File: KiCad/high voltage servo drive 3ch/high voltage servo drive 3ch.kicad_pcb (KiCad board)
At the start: 4 copper layers, 111.2 x 227 mm, 483 parts, among them J1 8P8C_LED_Shielded_x2, J3 Conn_ARM_SWD_TagConnect_TC2030, J4 MOTOR_A, J5 MOTOR_B, J6 MOTOR_C, J7 DC BUS, J8 STO, M1 Fan_4pin, Q1 BSS83P, U1 STM32G473QET6, U10 TPS54202DDC, U11 TPS54202DDC, U12 OPA4323IPWR, U13 OPA4323IPWR, U14 OPA4323IPWR, U15 PC-817S1-CTP1-F, U16 PC-817S1-CTP1-F, U17 IPM, U18 IPM, U19 PC-817S1-CTP1-F, U2 IPM, U3 MAX13433EESD, U4 MAX13433EESD, U5 CA_IS3741HW, U6 R24C2T25-R, U7 CA_IS3741HW, U8 CA_IS3741HW, U9 74LVC1G126, X1 SG-8002CE

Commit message: prepare rev0.1 for manufacturing
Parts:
- removed C137: 2.2uf, Capacitor_SMD:C_1206_3216Metric
- removed C45: 22uf, Capacitor_SMD:CP_Elec_6.3x5.9
- removed C46, C47: .1uf, Capacitor_SMD:C_0402_1005Metric
- removed C48: 75pf, Capacitor_SMD:C_0402_1005Metric
- removed C49, C50, C51: 22uf, Capacitor_SMD:C_1206_3216Metric
- removed C52: 220pf, Capacitor_THT:C_Disc_D9.0mm_W5.0mm_P10.00mm
- removed FB3, FB4: FerriteBead, Inductor_SMD:L_0805_2012Metric
- removed H1, H2, H3, H4, H5, H6, H7, H8, H9: MountingHole, footprints:MountingHole_3.2mm_M3
- removed L6: 15uH, Inductor_SMD:L_Taiyo-Yuden_MD-4040
- removed R16: 68.1k, Resistor_SMD:R_0402_1005Metric
- removed R25: 500k, Resistor_SMD:R_0402_1005Metric
- removed R26, R27: 100k, Resistor_SMD:R_0402_1005Metric
- removed R28: 13.3k, Resistor_SMD:R_0402_1005Metric
- removed U11: TPS54202DDC, Package_TO_SOT_SMD:SOT-23-6
- added C204: 22uf, Capacitor_SMD:C_1206_3216Metric, F.Cu at (190.2, 262.9)
- added C205: .1uf, Capacitor_SMD:C_0402_1005Metric, F.Cu at (196.4, 251.6)
- added C206: 22uf, Capacitor_SMD:C_1206_3216Metric, F.Cu at (195.5, 265.2)
- added C207: .1uf, Capacitor_SMD:C_1812_4532Metric, F.Cu at (189.5, 244.8)
- added D52: ES1J, Diode_SMD:D_SMA, F.Cu at (188.2, 251.4)
- added D53: ES1J, Diode_SMD:D_SMA, F.Cu at (194.9, 262.1)
- added D54: LED, LED_SMD:LED_0603_1608Metric, F.Cu at (245.1, 96.6)
- added L9: L, Inductor_THT:L_Radial_D7.2mm_P3.00mm_Murata_1700, B.Cu at (192.5, 258.5)
- added PS1: F0505S-1W, footprints:Converter_DCDC_FXXS-1W, B.Cu at (229.0, 56.9)
- added R150: 10k, Resistor_SMD:R_0402_1005Metric, F.Cu at (197.5, 253.7)
- added R151: 120, Resistor_SMD:R_0402_1005Metric, F.Cu at (252.4, 119.7)
- added R152: 1k, Resistor_SMD:R_0402_1005Metric, F.Cu at (196.4, 253.7)
- added R153: 0, Resistor_SMD:R_0402_1005Metric, F.Cu at (224.3, 58.6)
- added R154: 0, Resistor_SMD:R_0402_1005Metric, F.Cu at (222.8, 57.1)
- added R155: 0, Resistor_SMD:R_0402_1005Metric, F.Cu at (222.8, 55.6)
- added R156: 0, Resistor_SMD:R_0402_1005Metric, F.Cu at (226.4, 54.9)
- added REF**: Symbol_HighVoltage_Triangle_8x7mm_Silk, EO logos:Symbol_HighVoltage_Triangle_8x7mm_Silk, F.Cu at (177.3, 200.6)
- added REF**: Symbol_HighVoltage_Triangle_8x7mm_Silk, EO logos:Symbol_HighVoltage_Triangle_8x7mm_Silk, B.Cu at (259.4, 199.1)
- added REF**: Symbol_HighVoltage_Triangle_8x7mm_Silk, EO logos:Symbol_HighVoltage_Triangle_8x7mm_Silk, B.Cu at (192.9, 270.2)
- added REF**: Symbol_HighVoltage_Triangle_8x7mm_Silk, EO logos:Symbol_HighVoltage_Triangle_8x7mm_Silk, F.Cu at (186.9, 82.8)
- added REF**: Symbol_HighVoltage_Triangle_8x7mm_Silk, EO logos:Symbol_HighVoltage_Triangle_8x7mm_Silk, F.Cu at (260.0, 104.8)
- added REF**: Symbol_HighVoltage_Triangle_8x7mm_Silk, EO logos:Symbol_HighVoltage_Triangle_8x7mm_Silk, F.Cu at (169.2, 267.4)
- added REF**: EO silk 14mm, EO logos:EO silk 14mm, F.Cu at (176.7, 78.7)
- added REF**: OSHW-Logo2_14.6x12mm_SilkScreen, Symbol:OSHW-Logo2_14.6x12mm_SilkScreen, F.Cu at (164.0, 87.3)
- added REF**: Symbol_HighVoltage_Triangle_8x7mm_Silk, EO logos:Symbol_HighVoltage_Triangle_8x7mm_Silk, B.Cu at (251.6, 72.1)
- added REF**: OSHW-Logo2_14.6x12mm_SilkScreen, Symbol:OSHW-Logo2_14.6x12mm_SilkScreen, B.Cu at (241.3, 53.6)
- added REF**: EO silk 14mm, EO logos:EO silk 14mm, B.Cu at (255.9, 52.9)
- added TP3: 5V, TestPoint:TestPoint_Pad_D2.0mm, F.Cu at (245.0, 94.1)
- added U20: LNK306D, Package_SO:PowerIntegrations_SO-8C, F.Cu at (193.1, 251.3)
- added U21: TLV75733PDBV, Package_TO_SOT_SMD:SOT-23-5, F.Cu at (246.9, 105.6)
- C101, C107, C109, C56, C57, C64, C70, C76, C82, C88, C90, C95: value 0.1uf -> .1uf
- C127: value 75pf -> 100pf
- C130: footprint Capacitor_THT:C_Rect_L18.0mm_W11.0mm_P15.00mm_FKS3_FKP3 -> Capacitor_THT:C_Rect_L26.5mm_W10.5mm_P22.50mm_MKS4
- C24: value 330pf -> 22uf; footprint Capacitor_SMD:C_0402_1005Metric -> Capacitor_SMD:C_1206_3216Metric
- C39, C40: value .1uf -> 22uf; footprint Capacitor_SMD:C_0402_1005Metric -> Capacitor_SMD:C_1206_3216Metric
- C41: value 2.2uf -> 22uf
- D10: value 24V_ISO_ON -> LED
- D11: value GATE_SUPPLY_ON -> LED
- D12: value 3.3V_ON -> LED
- D31: value 3.3VA_ON -> LED
- D33: value LED_0 -> LED
- D36: value STO_CH_1 -> LED
- D39: value STO_CH_2 -> LED
- D50: value STO_FBK -> LED
- D51: value LED_1 -> LED
- D9: value 5V_ISO_ON -> LED
- FB1, FB10, FB2, FB5, FB6, FB7, FB8, FB9: value FerriteBead -> 0
- L5: footprint Inductor_SMD:L_Taiyo-Yuden_MD-4040 -> footprints:CY54_INDUCTOR
- R1, R100, R101, R102, R103, R104, R105, R107, R114, R115, R116, R117, R118, R119, R121, R2, R3, R4, R5, R6, R8: value 100 -> 120
- R15: value 11k -> 1k
- R23: value 500k -> 560k
- R33, R34, R38, R39, R43, R44, R48, R49, R53, R54, R58, R59, R63, R64, R68, R69, R73, R74: value 1k -> 1k
- R35, R36, R40, R41, R45, R46, R50, R51, R55, R56, R60, R61, R65, R66, R70, R71, R75, R76: value 12.1 -> 12.1k
- U6: value R24C2T25-R -> TLV75733PDBV; footprint footprints:36L-SSOP_RCP -> Package_TO_SOT_SMD:SOT-23-5
- X1: value SG-8002CE -> 16Mhz
- moved D11 157.8 mm to (198.0, 270.5)
- moved TP1 154.7 mm to (197.6, 268.1)
- moved R31 154.3 mm to (199.1, 266.0), turned to 90 degrees
- moved C41 45.0 mm to (250.5, 105.6), turned to 90 degrees
- moved U6 42.7 mm to (246.9, 99.8), turned to 0 degrees
- moved C39 39.1 mm to (250.5, 99.8), turned to 90 degrees
- moved C24 35.9 mm to (242.8, 102.7), turned to 90 degrees
- moved R15 31.4 mm to (247.3, 95.0), turned to 90 degrees
- moved R78 24.5 mm to (246.6, 119.4)
- moved D31 24.5 mm to (246.5, 121.0)
- moved TP7 24.5 mm to (243.4, 121.0)
- moved C130 18.5 mm to (182.7, 269.9), turned to 180 degrees
- moved R32 15.2 mm to (245.6, 116.8)
- moved D12 15.2 mm to (246.4, 115.0)
- moved TP6 15.2 mm to (243.3, 115.0)
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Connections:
- C24 pad 2: Net-(U6-FBVOUT+) -> +5VP
- C35 pad 1: +24V -> Net-(M1-+)
- C38 pad 2: +24V -> Net-(PS1-+Vin)
- C39 pad 2: +GATE_SUPPLY -> Net-(U6-OUT)
- C40 pad 1: GND -> GND1
- C40 pad 2: +24V -> +5VP
- C41 pad 2: +GATE_SUPPLY -> +3.3V
- M1 pad 2: +24V -> Net-(M1-+)
- R15 pad 1: GND1 -> Net-(D54-A)
- R15 pad 2: Net-(U6-FBVOUT+) -> +5VP
- U6 pad 1: GND -> +5VP
- U6 pad 2: GND -> GND1
- U6 pad 3: unconnected-(U6-PG-Pad3) -> +5VP
- U6 pad 5: GND -> Net-(U6-OUT)
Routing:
- net +5VP: track 0.00 -> 60.7 mm
- net Net-(U6-OUT): track 0.00 -> 31.8 mm
- net +GATE_SUPPLY: track 208.5 -> 236.0 mm, vias 8 -> 9
- net GND: track 73.2 -> 50.0 mm, vias 39 -> 30
- net +24V: track 123.7 -> 102.0 mm, vias 4 -> 3
- net Net-(D53-K): track 0.00 -> 17.4 mm, vias 0 -> 2
- net Net-(M1-+): track 0.00 -> 15.9 mm, vias 0 -> 2
- net Net-(U20-FB): track 0.00 -> 10.4 mm
- net Net-(C48-Pad2): track 10.3 -> 0.00 mm
- net Net-(U6-FBVOUT+): track 8.66 -> 0.00 mm
- net Net-(U11-FB): track 8.34 -> 0.00 mm
- net +3.3VA: track 149.0 -> 157.3 mm
- net GND1: track 286.0 -> 278.8 mm, vias 726 -> 745
- net Net-(PS1-+Vin): track 0.00 -> 6.74 mm
- net Net-(U11-EN): track 6.44 -> 0.00 mm
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- added copper zone on F.Cu, net Net-(D52-K)
- removed copper zone on F.Cu, net +GATE_SUPPLY
- removed copper zone on B.Cu, net Net-(C48-Pad2)
- removed copper zone on F.Cu, net Net-(C48-Pad2)
- removed copper zone on F.Cu, net Net-(U11-SW)
- removed copper zone on In2.Cu, net Net-(U11-SW)
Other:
- board size 111.2 x 227 mm -> 109 x 231.4 mm
- board text added: "####"
- board text added: "+3.3V"
- board text added: "+3.3VA"
- board text added: "+5V"
- board text added: "+5VP"
- board text added: "+GATE SUPPLY"
- board text added: "A"
- board text added: "A_U"
- board text added: "A_V"
- board text added: "A_W"
- board text added: "B"
- board text added: "B_U"
- board text added: "B_V"
- board text added: "B_W"
- board text added: "C"
- board text added: "C_U"
- board text added: "C_V"
- board text added: "C_W"
- board text added: "GND"
- board text added: "GND1"
- board text added: "HVSD-35/400-3"
- board text added: "PROGRAMMER IS NOT ISOLATED FROM HV!"
- board text added: "PWM"
- board text added: "REV 0.1"
- board text added: "STLINK"
- board text added: "TACH"
- board text added: "U1"
- board text added: "V+"
- board text added: "VBUS"
- board text added: "VIN+"
- board text added: "VIN-"
- board text added: "WARNING HIGH VOLTAGE"
- board text removed: "CH1"
- board text removed: "CH2"
- board text removed: "FBK"

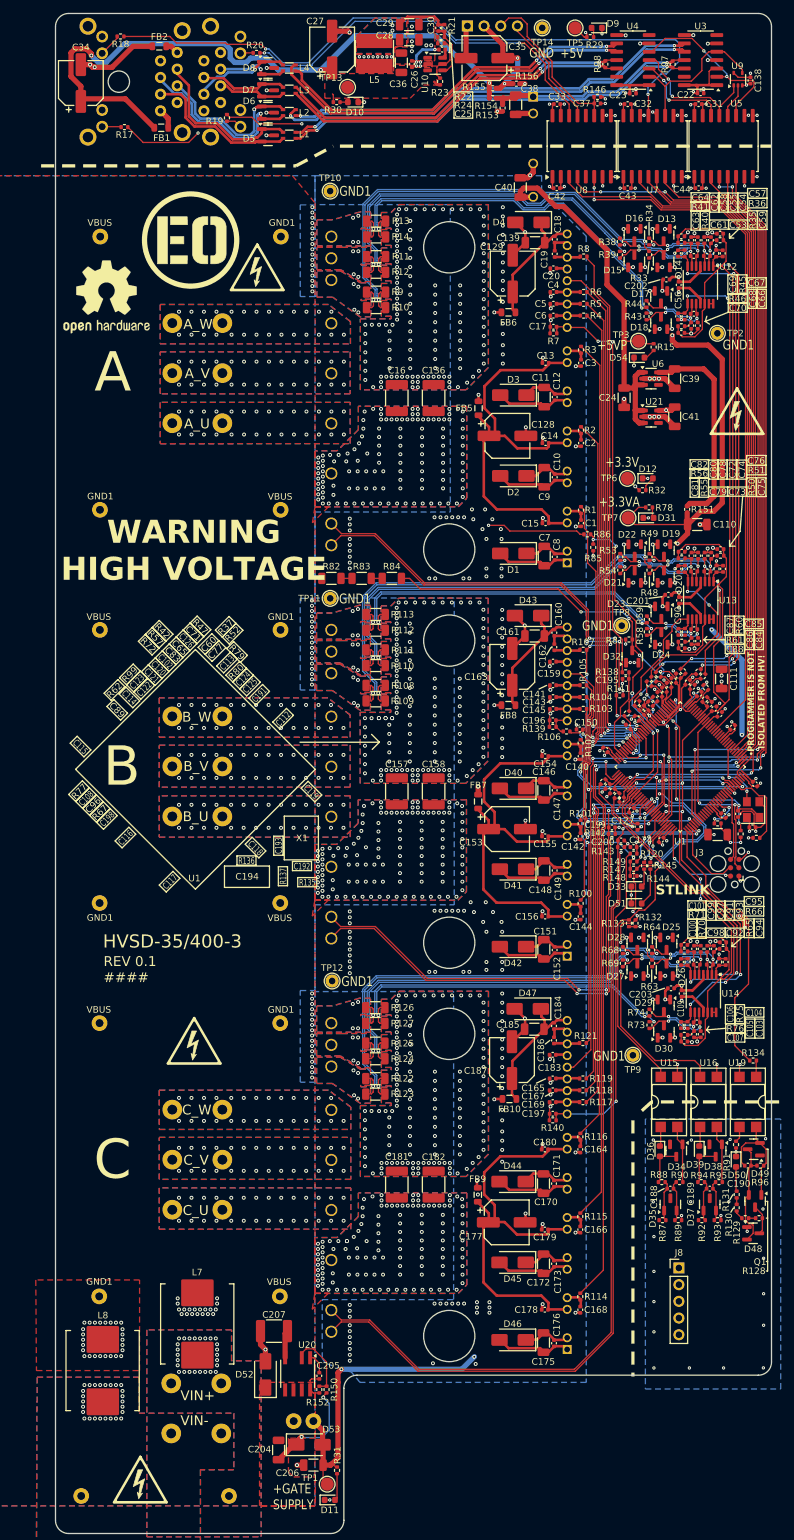
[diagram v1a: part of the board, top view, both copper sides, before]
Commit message: fix DRC issues
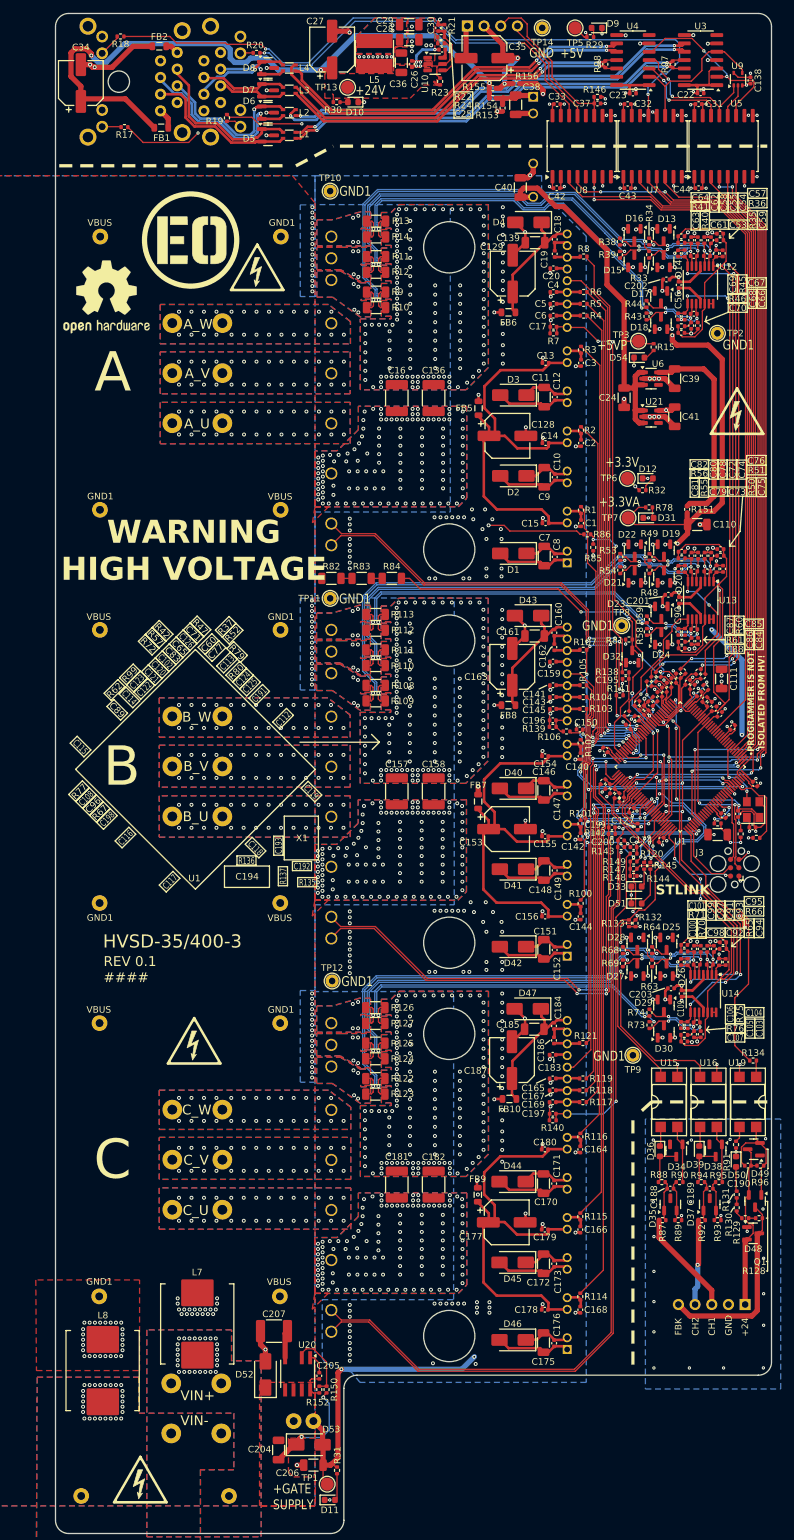
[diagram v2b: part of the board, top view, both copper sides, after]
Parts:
- C131, C132, C133, C134, C135, C21: footprint footprints:C_Rect_L32mm_W18.0mm_P27.50mm_MKS4 -> footprints:C_Rect_L32mm_W16.0mm_P27.50mm
- J8: moved to B.Cu
- moved J8 11.5 mm to (261.2, 240.8), turned to 90 degrees
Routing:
- net /STO/FBK: track 4.62 -> 29.6 mm
- net /STO/CH1: track 0.00 -> 16.2 mm
- net /STO/CH2: track 0.00 -> 13.1 mm, vias 0 -> 1
- net +24V_STO: track 16.4 -> 26.4 mm
- net +5V: track 44.0 -> 41.4 mm, vias 15 -> 16
- net +GATE_SUPPLY: track 236.0 -> 234.5 mm
- net /Microcontroller/VREF_FULL: track 18.8 -> 20.0 mm
- net +24V: track 102.0 -> 101.0 mm
- net Net-(U20-FB): track 10.4 -> 9.65 mm
- net +5VP: track 60.7 -> 60.1 mm
- net /Microcontroller/SWDIO: track 13.7 -> 14.2 mm
- net +3.3VA: track 157.3 -> 157.2 mm, vias 28 -> 27
- net GND1: track 278.8 -> 278.9 mm, vias 745 -> 741
- net VBUS: vias 392 -> 391
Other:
- board text added: "+24"
- board text added: "+24V"
- board text added: "+V"
- board text added: "CH1"
- board text added: "CH2"
- board text added: "FBK"
- board text removed: "V+"
